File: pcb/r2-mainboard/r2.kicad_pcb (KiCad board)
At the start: 4 copper layers, 88.2 x 106.2 mm, 331 parts, among them J1 USB-C 16P, J2 Pico-Lock 504050-0391, J20 SWD+JTAG (DNP), J21 MICRO_SD(TFC-WPAPR-08), J22 HC-FPC-05-09-6RLTAG, J23 HC-FPC-05-09-6RLTAG, J24 HC-FPC-05-09-8RLTAG, J25 SolderPads 3x, J26 BTH-060-01-L-D-A-K-TR, J27 BTH-060-01-L-D-A-K-TR, J28 USB-C 16P, J6 XF2M-4015-1A, Q1 AO3401A, Q2 S8050, Q6 AO3400A, Q7 AO3401A, Q8 AO3401A, Q9 AO3400A, SW20 EVQPUC02K, SW21 SW, SW22 SW, U1 BQ25892RTW, U10 TPS7A0233DBVR, U12 TPS61022RWUR, U13 TPS63802DLAR, U14 TPS62A02DRLR, U15 TPS62A02DRLR, U2 MAX17048G+T10, U20 STM32G0B1RCT6, U21 INA3221, U22 INA3221, U23 LGS6302B5, U24 LGS6302B5, U26 LGS5145, U27 INA3221, U3 USBLC6-2SC6, U31 LM321, U41 XC6SLX-FTG256, U42 W25Q128JVSIQ, U52 MT41K64M16TW, U53 LM3630A, U54 TPS22914BYFPR, U55 TPS22914BYFPR, U56 TPS2553DBVR, U57 USBLC6-2SC6, U6 MT9700, U7 TPS22914BYFPR, U8 TPS22914BYFPR, U9 LGS5145, X1 33.33MHz, X2 PCM-071, Y20 32.768kHz

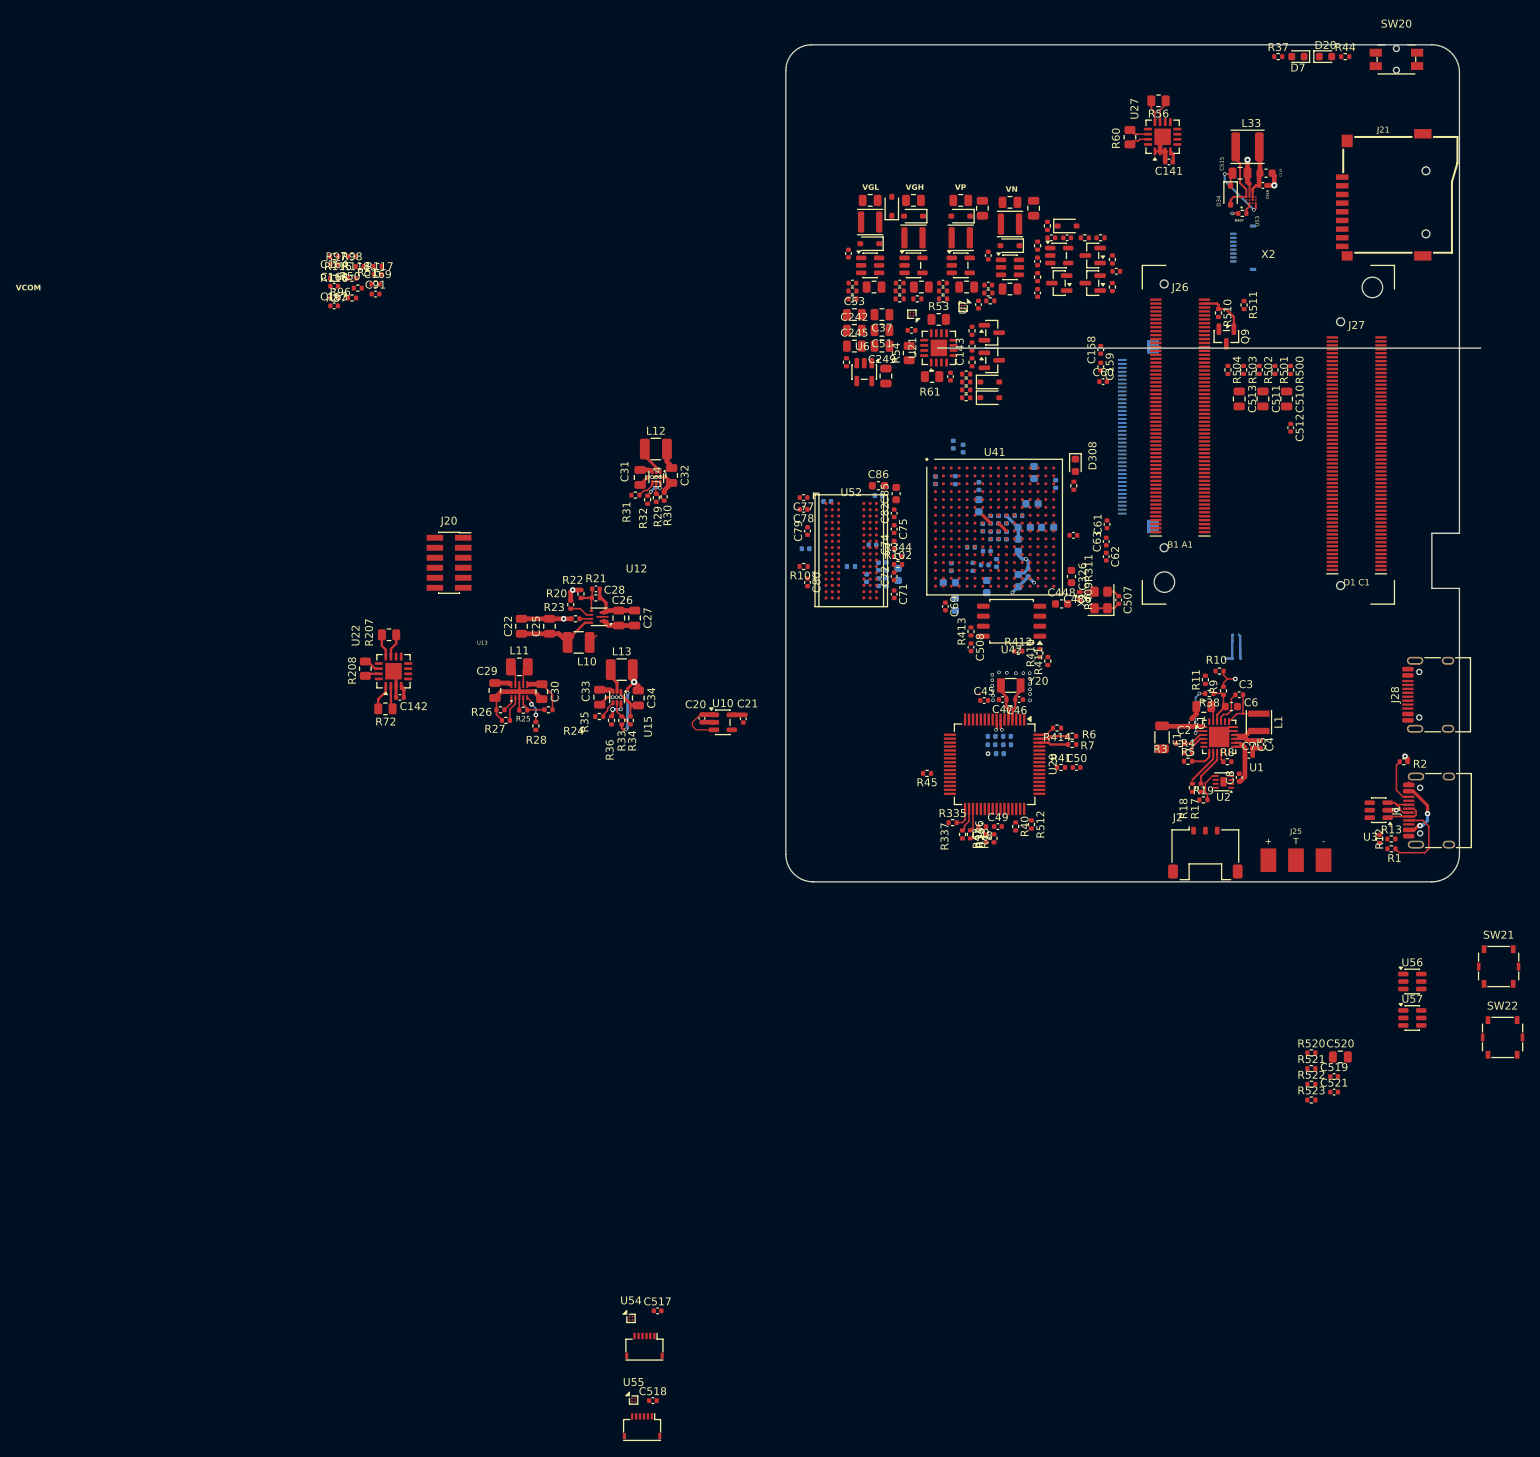
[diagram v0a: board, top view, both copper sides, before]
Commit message: Touch decided: I2C hand-wired for the prototype; Caster bitgen applied
Good Display's answer of 2026-08-31 closes the on-board GT9110H idea:
the driving board is another customer's design and they will not share
files, so the panel's ITO channel map is unobtainable at prototype
scale. The production path is now priced instead -- US$750 tooling,
MOQ 1000/lot, for a custom panel with the interface and touch IC of our
choosing.

Owner's decision: option C. Touch runs over I2C on J22, hand-wired to
the vendor board's test points for the prototype. USB was rejected --
USB0 is the charge port and USB1 is now the host port, so USB touch
would have needed a hub and would have cost touch-to-wake permanently.
No schematic change: J22/J23 and U54/U55 stay exactly as drawn, DNP.

io-expansion.md 5.2 records the decision and the three firmware ways to
disable touch-to-wake; 5.3 records a real gap found on the vendor board
-- it exposes SDA/SCL/VDD/GND/DBG/INT/DP and *no* RST pad, so reset
becomes a power cycle through MCU_EN_TOUCH, and the GT9110's I2C
address cannot be selected and must be scanned for at bring-up.

Also in this commit, the owner's work: Caster bitgen at ConfigRate 22 /
x4 / binary (submodule pointer bump), epd_power and io_expansion sheet
edits, and board layout.

Co-Authored-By: Claude Opus 5 <noreply@anthropic.com>
Claude-Session: https://claude.ai/code/session_01MHTAe6ZnhogTEgtyPcLhwG
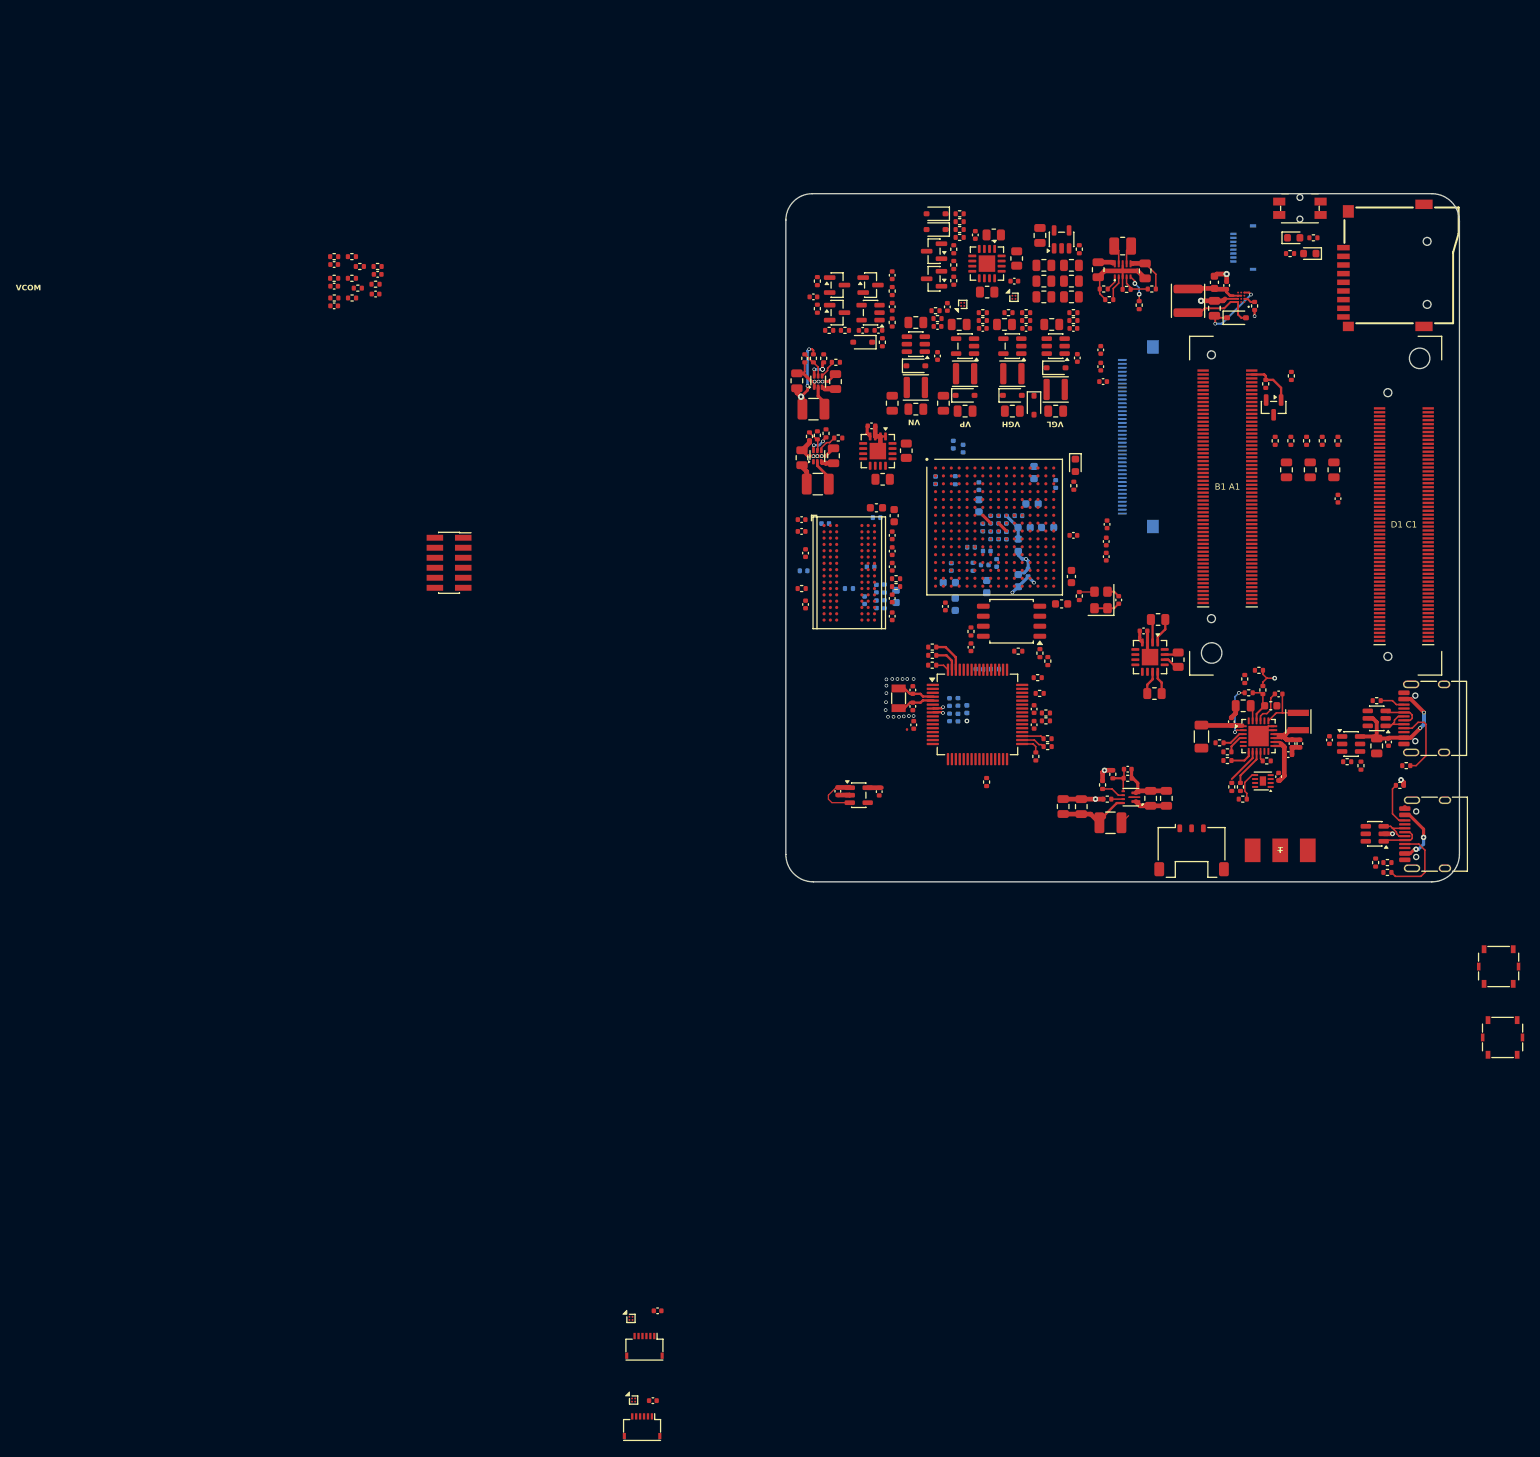
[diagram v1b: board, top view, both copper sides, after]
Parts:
- C50, R41: moved to B.Cu
- moved R208 103.2 mm to (236.8, 96.5), turned to 90 degrees
- moved R72 98.7 mm to (234.2, 91.5), turned to 180 degrees
- moved R207 97.4 mm to (233.8, 100.8), turned to 0 degrees
- moved U22 96.0 mm to (233.2, 96.2), turned to -90 degrees
- moved C142 94.8 mm to (232.4, 92.9), turned to 0 degrees
- moved R27 93.4 mm to (228.1, 50.9)
- moved C29 93.4 mm to (226.7, 47.0)
- moved L11 93.4 mm to (229.8, 44.0)
- moved R25 93.4 mm to (230.2, 49.5)
- moved U13 93.4 mm to (229.8, 47.0)
- moved C30 93.4 mm to (232.6, 47.2)
- moved R24 93.4 mm to (233.4, 49.5)
- moved R26 93.4 mm to (227.3, 49.5)
- moved R28 93.4 mm to (231.8, 51.5)
- moved C22 72.5 mm to (222.2, 115.2)
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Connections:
- J28 pad A6: /USB1_DP -> /io_expansion/USB1_D+
- J28 pad A7: /USB1_DM -> /io_expansion/USB1_D-
- J28 pad B6: /USB1_DP -> /io_expansion/USB1_D+
- J28 pad B7: /USB1_DM -> /io_expansion/USB1_D-
- U57 pad 1: /USB1_DM -> /io_expansion/USB1_D-
- U57 pad 3: /USB1_DP -> /io_expansion/USB1_D+
- U57 pad 4: /USB1_DP -> /io_expansion/USB1_+
- U57 pad 6: /USB1_DM -> /io_expansion/USB1_D-
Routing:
- net /USB1_VBUS: track 0.00 -> 17.1 mm, vias 0 -> 2
- net Net-(J28-CC1): track 0.00 -> 9.72 mm
- net /io_expansion/USB1_D+: track 0.00 -> 5.16 mm
- net /io_expansion/USB1_D-: track 0.00 -> 4.43 mm
- net +3V3_AON: track 10.6 -> 6.47 mm
- net /mcu/+3V3_VREF: track 4.49 -> 1.33 mm
- net Net-(J28-CC2): track 0.00 -> 3.15 mm
- net +1V5: track 3.00 -> 0.00 mm
- net +1V5_DCDC: track 13.4 -> 10.5 mm
- net +1V2_DCDC: track 5.20 -> 2.65 mm
- net +1V2_FPGA: track 8.91 -> 6.40 mm
- net GND: track 76.7 -> 75.4 mm, vias 20 -> 22
- net +VSYS: track 36.3 -> 35.1 mm
- net /SCL_AON: track 3.75 -> 4.59 mm
- net +3V3: vias 13 -> 11
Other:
- board size 88.2 x 106.2 mm -> 85.5 x 87.3 mm

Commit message: Docs: library audit list and a first production costing
libraries.md -- every symbol in r2.kicad_sym and every footprint in
r2.pretty, with what it was derived from, which tools/ script emits it,
and what was actually checked. Written for the owner's audit before the
libraries get rehomed. Notes that pcb_common has never been modified,
and calls out the three newest entries (TPS2553DBV and the two
_Mirrored FPC land patterns) as the least reviewed.

NOTES-production-costing.md -- what 1000 units costs and what a campaign
would have to raise, prompted by Good Display's US$750 / MOQ 1000 quote.
Central estimate EUR 340/unit COGS and a EUR ~548k goal, but the honest
finding is the sensitivity: the PCM-071 at EUR 250 @1-9 costs more than
the display, and the sibling quote says ~EUR 190 of that is a memory-
shortage surcharge. A 1000-piece quote moves the goal by EUR 290k, so it
is the single highest-value thing to chase. Also states plainly that at
the central estimate the margin is thin to negative against market
comparables, and what to do about it.

Both indexed in CLAUDE.md.

Co-Authored-By: Claude Opus 5 <noreply@anthropic.com>
Claude-Session: https://claude.ai/code/session_01MHTAe6ZnhogTEgtyPcLhwG
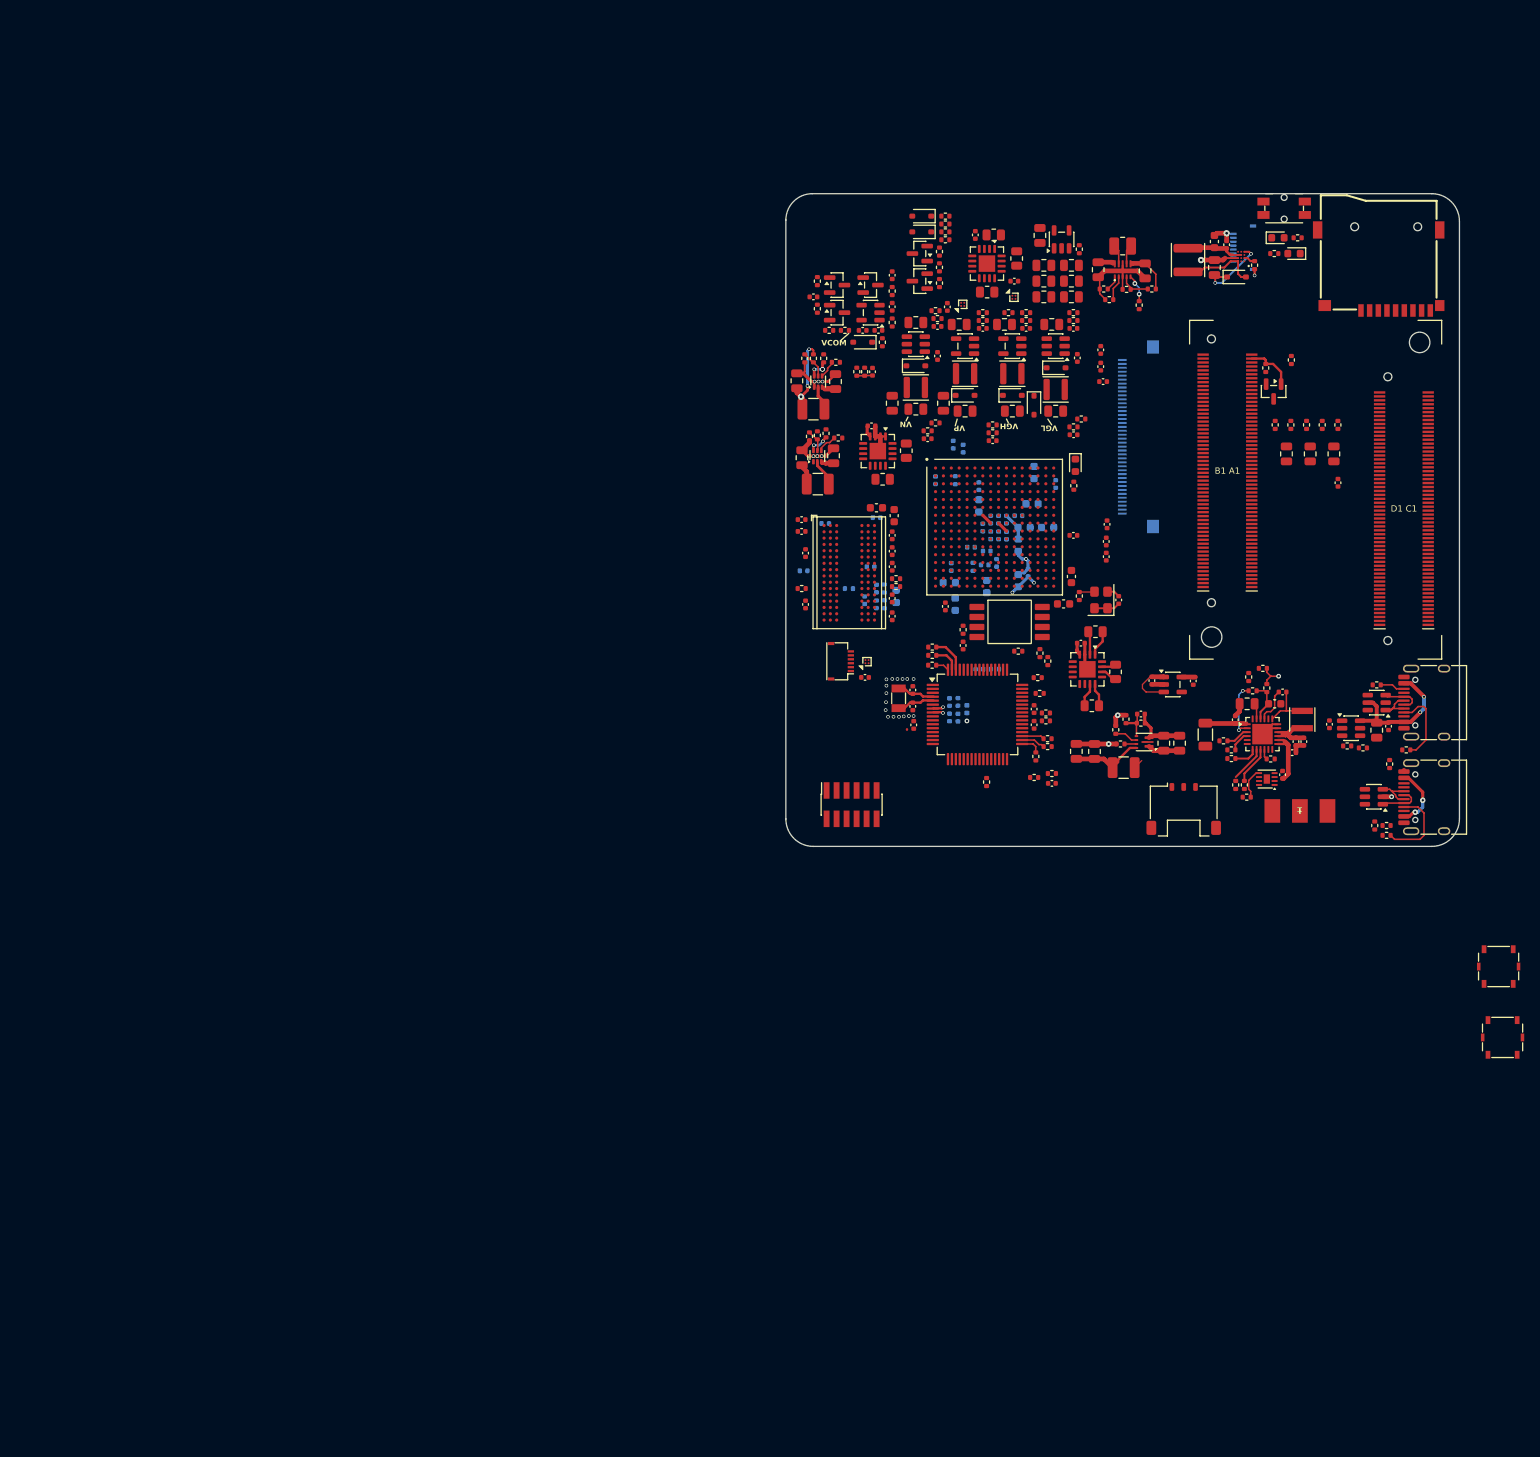
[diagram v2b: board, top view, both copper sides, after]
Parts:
- removed C518: 1uF/16V, Capacitor_SMD:C_0402_1005Metric
- removed J23: HC-FPC-05-09-6RLTAG, footprints:HC-FPC-05-09-6RLTAG
- removed U42: W25Q128JVSIQ, Package_SO:SOIC-8_5.3x5.3mm_P1.27mm
- removed U55: TPS22914BYFPR, Package_BGA:WLP-4_0.83x0.83mm_P0.4mm
- added U902: W25Q128JVSIQ, Reflow:QSPI Flash SOIC, F.Cu at (215.4, 91.8)
- moved C91 106.0 mm to (220.8, 112.2)
- moved R50 106.0 mm to (218.5, 111.5)
- moved R51 106.0 mm to (220.8, 111.0)
- moved R118 93.6 mm to (224.5, 66.0), turned to 0 degrees
- moved J22 90.7 mm to (193.6, 96.8), turned to -90 degrees
- moved C169 90.6 mm to (223.5, 68.0)
- moved R117 90.6 mm to (223.5, 67.0), turned to 0 degrees
- moved U54 88.6 mm to (197.3, 96.8), turned to 90 degrees
- moved C164 86.5 mm to (213.2, 68.8), turned to 180 degrees
- moved R97 86.5 mm to (213.2, 67.8), turned to 180 degrees
- moved C517 84.6 mm to (197.1, 98.8)
- moved R98 84.1 mm to (213.2, 66.8)
- moved R116 78.5 mm to (206.0, 66.5), turned to 0 degrees
- moved C168 77.8 mm to (205.0, 68.5)
- moved R115 75.6 mm to (205.0, 67.5), turned to 0 degrees
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- renumbered J1 to J200, J2 to J201, J25 to J202, U1 to U200, U2 to U201, U10 to U300, U12 to U301, U13 to U302, U14 to U303, U15 to U304
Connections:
- C517 pad 1: /io_expansion/+3V3_TOUCH -> Net-(U54-OUT)
- U54 pad A1: /io_expansion/+3V3_TOUCH -> Net-(U54-OUT)
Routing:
- net /battery/USB_CC2: track 5.70 -> 0.00 mm
- net /VP_MEA: track 0.00 -> 2.01 mm
- net GND: track 75.4 -> 74.6 mm, vias 22 -> 25
- net +3V3: vias 11 -> 7
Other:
- board size 85.5 x 87.3 mm -> 85.5 x 82.8 mm
